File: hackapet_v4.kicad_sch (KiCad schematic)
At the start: 43 parts, among them J1 Conn_01x02_Socket, J4 USB_C_Receptacle_USB2.0_16P, J7 lipo, Q1 AO3401A, SW1 SW_Push, SW2 SW_Push, SW3 SW_Push, SW4 SW_SPDT, U1 XC6206PxxxMR, U2 ESP-PSRAM32, U3 ESP32-S2-MINI-2, U9 TP4056-42-ESOP8

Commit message: routed!
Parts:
- removed C22, C23: 10u, Capacitor_SMD:C_0805_2012Metric, symbol Device:C_Small
- removed D13: LED, LED_SMD:LED_0805_2012Metric, symbol Device:LED
- removed D15: MBR0530, Diode_SMD:D_SOD-123, symbol Diode:MBR0530
- removed D2, D6, D8: S-LMBR340FT1G, Diode_SMD:D_0805_2012Metric, symbol Device:D
- removed Q1: AO3401A, Package_TO_SOT_SMD:SOT-23, symbol Transistor_FET:AO3401A
- removed R39, R44: 1.5k, Resistor_SMD:R_0805_2012Metric, symbol Device:R_Small
- removed R43: 5.1k, Resistor_SMD:R_0805_2012Metric, symbol Device:R_Small
- removed U9: TP4056-42-ESOP8, Package_SO:SOIC-8-1EP_3.9x4.9mm_P1.27mm_EP2.41x3.3mm_ThermalVias, symbol Battery_Management:TP4056-42-ESOP8
- added C6: 1uF, Capacitor_SMD:C_0805_2012Metric, symbol Device:C_Small
- added C7, C8: 4u7, Capacitor_SMD:C_0805_2012Metric, symbol Device:C_Small
- added D1: LED, LED_SMD:LED_0805_2012Metric, symbol Device:LED_Small
- added Q2: 2N7002, Package_TO_SOT_SMD:SOT-23, symbol Transistor_FET:2N7002
- added R11, R8: 1k5, Resistor_SMD:R_0805_2012Metric, symbol Device:R_Small
- added R12: 3k9, Resistor_SMD:R_0805_2012Metric, symbol Device:R_Small
- added R13: 100R, Resistor_SMD:R_0805_2012Metric, symbol Device:R_Small
- added R14, R9: 10k, Resistor_SMD:R_0805_2012Metric, symbol Device:R_Small
- added R15: 100k, Resistor_SMD:R_0805_2012Metric, symbol Device:R_Small
- added U11: SRV05-4, Package_TO_SOT_SMD:SOT-23-6, symbol Power_Protection:SRV05-4
- added U4: BQ24075RGT, Package_DFN_QFN:VQFN-16-1EP_3x3mm_P0.5mm_EP1.6x1.6mm, symbol Battery_Management:BQ24075RGT
- C3: value 0.1uF -> 4u7; LCSC C28378 -> (none)
- C5: value 10uF -> 1uF
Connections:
- net +3V3: now also C4.1, C5.1, U1.2 (VO)
- net +5V: now also C3.1, U1.3 (VI), C6.1, D1.2 (A), U4.10 (OUT), U4.11 (OUT), U4.6 (EN1)
- net +BATT: now also J7.1 (Pin_1), C7.1, R15.1, U4.2 (BAT), U4.3 (BAT); no longer SW4.2 (B)
- net D+: now also U11.3 (IO2), U11.4 (IO3)
- net D-: now also U11.1 (IO1), U11.6 (IO4)
- net GND: now also C1.2, C3.2, SW4.3 (C), C6.2, C7.2, C8.2, Q2.2 (S), R11.2, R12.2, R14.2, R9.2, U11.2 (VN), U4.17 (VSS), U4.4 (~{CE}), U4.5 (EN2), U4.8 (VSS); no longer C1.1, C3.1
- net VBUS: now also C1.1, J4.A4 (VBUS), J4.A9 (VBUS), J4.B4 (VBUS), J4.B9 (VBUS), C8.1, R13.1, U11.5 (VP), U4.13 (IN); no longer U1.3 (VI)
- net at SW4.1 (A): now also R15.2; no longer J7.1 (Pin_1)
- new net: Q2.1 (G), R13.2, R14.1
- new net: D1.1 (K), R8.1
- new net: R8.2, U4.9 (~{CHG})
- new net: R11.1, U4.12 (ILIM)
- new net: R9.1, U4.1 (TS)
- new net: R12.1, U4.16 (ISET)
- new net SYSOFF: Q2.3 (D), SW4.2 (B), U4.15 (SYSOFF)
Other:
- note removed: "i hope 0402 works"
- moved on the sheet: C1, C4, C5, D3, D4, D5, D7, J1, J7, R1, R2, R3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

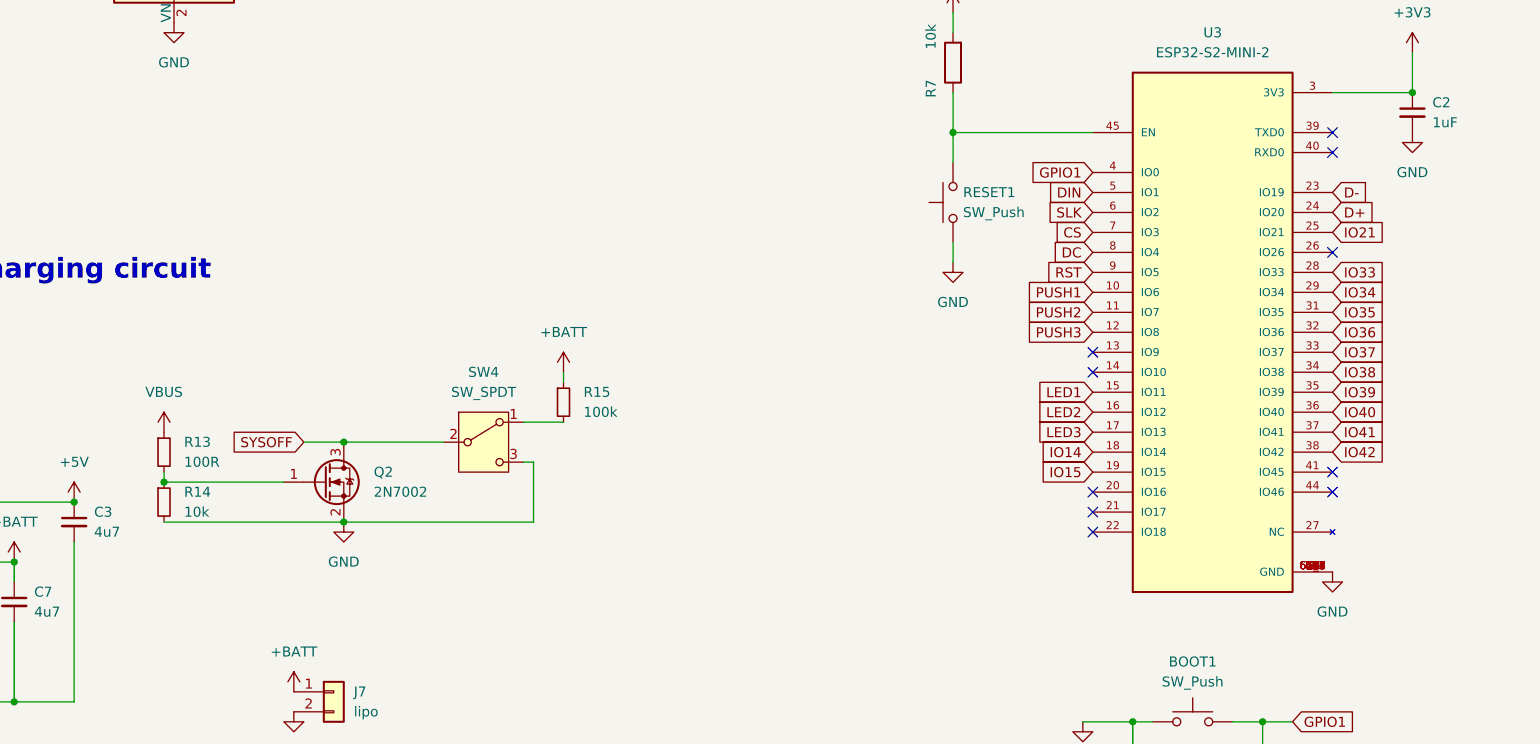
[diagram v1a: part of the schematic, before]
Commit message: add keepout, thicken 3v3 to .5
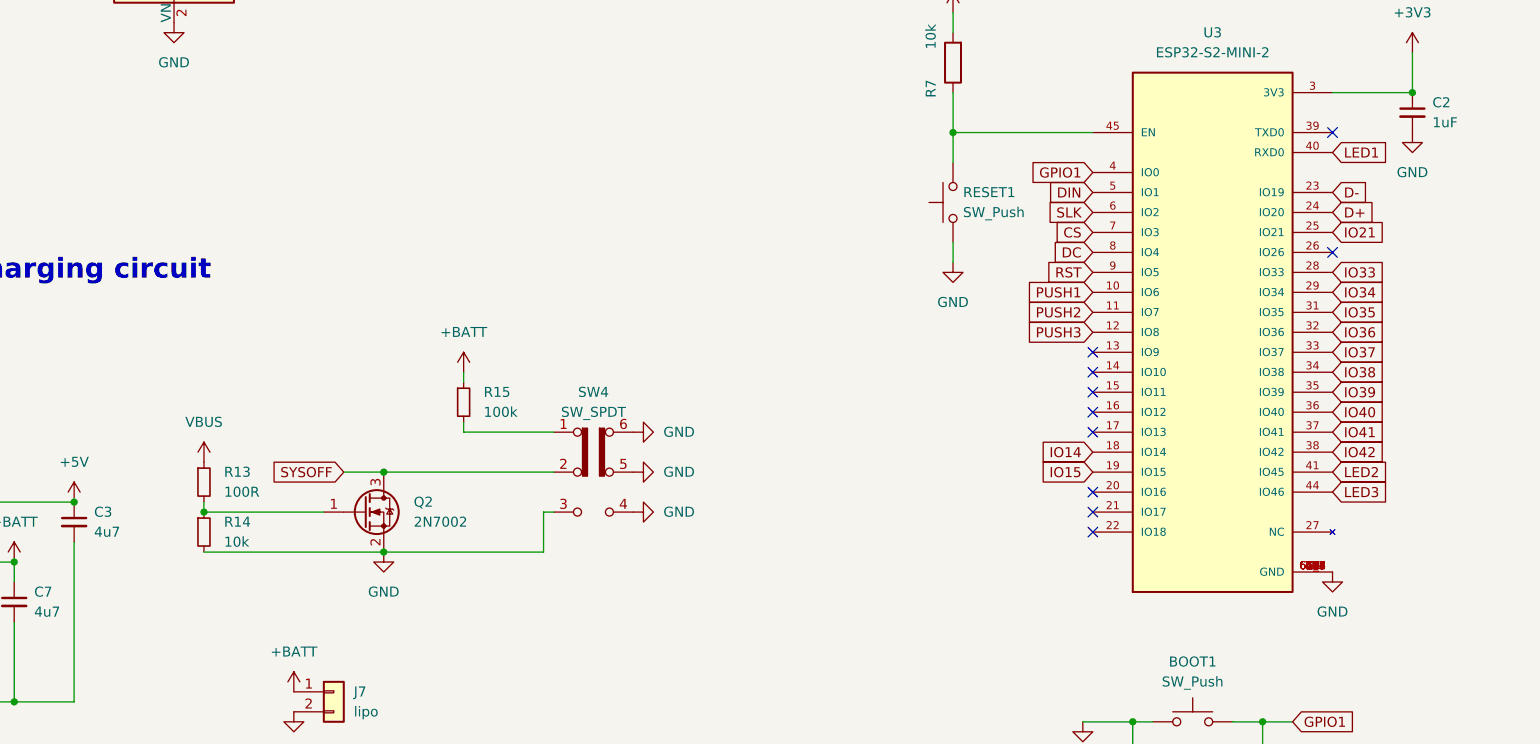
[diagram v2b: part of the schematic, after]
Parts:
- SW4: symbol Switch:SW_SPDT -> Switch:SW_Slide_DPDT
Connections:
- net GND: now also SW4.4 (A), SW4.5 (B), SW4.6 (C)
- net LED1: now also U3.40 (RXD0); no longer U3.15 (IO11)
- net LED2: now also U3.41 (IO45); no longer U3.16 (IO12)
- net LED3: now also U3.44 (IO46); no longer U3.17 (IO13)
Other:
- moved on the sheet: Q2, R13, R14, R15

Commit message: final updates!
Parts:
- added J2: breakout, Connector_PinHeader_2.54mm:PinHeader_1x02_P2.54mm_Vertical_SMD_Pin1Left, symbol Connector:Conn_01x02_Socket
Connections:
- net +BATT: now also J2.1 (Pin_1)
- net GND: now also J2.2 (Pin_2)
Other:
- moved on the sheet: J7
